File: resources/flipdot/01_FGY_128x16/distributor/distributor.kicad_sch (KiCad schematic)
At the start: 46 parts, among them J1 Conn_01x34, J2 Conn_01x28, J3 Conn_01x16, J4 Conn_01x16, U1 4049, U10 4051, U11 4051, U12 4051, U13 UDN2580, U14 UDN2580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

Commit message: Distributor board design files v0.2
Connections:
- net column_b3 renamed column_bank_b0
- net column_b4 renamed column_bank_b1
- net column_b5 renamed column_bank_b2
- net column_b6 renamed column_bank_b3
- net column_b6_{+1} renamed column_bank_b3_{+1}
- net column_e? renamed flip_enable
- net column_e?_{+1} renamed column_enable
- net column_~{b6}_{+1} renamed column_bank_~{b3}_{+1}
- net column_~{e}?_{+2} renamed row_bank_select_inh
- net mode_0? renamed model_select_0?
- net mode_1? renamed model_select_1?
- net mode_2? renamed model_select_2?
- net mode_3? renamed model_select_3?
- net mode_4? renamed model_select_4?
- net mode_5? renamed model_select_5?
- net mode_6? renamed model_select_6?
- net mode_7? renamed model_select_7?
- net row_bnk_0_inh renamed row_bank_0_inh
- net row_bnk_1_inh renamed row_bank_1_inh
- net row_bnk_2_inh renamed row_bank_2_inh
- net row_inhibit? renamed row_dir_source
- net row_inhibit?_{+1} renamed row_dir_drain
- net unk0 renamed column_dir_drain
- net unk1 renamed column_dir_source
- net unk2 renamed flip_dir
- net weird renamed row_bank_disable_all
- net weird_{+1} renamed row_bank_disable_all_{+1}
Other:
- note added: "VIBRATOR"
- note added: "[0..4]"
- note added: "[16..18]"
- note added: "[24..31]"
- note added: "[7..11]"
- note added: "[7]"
- moved on the sheet: C1, C10, C11, C12, C13, C2, C3, C4, C5, C7, C8, C9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

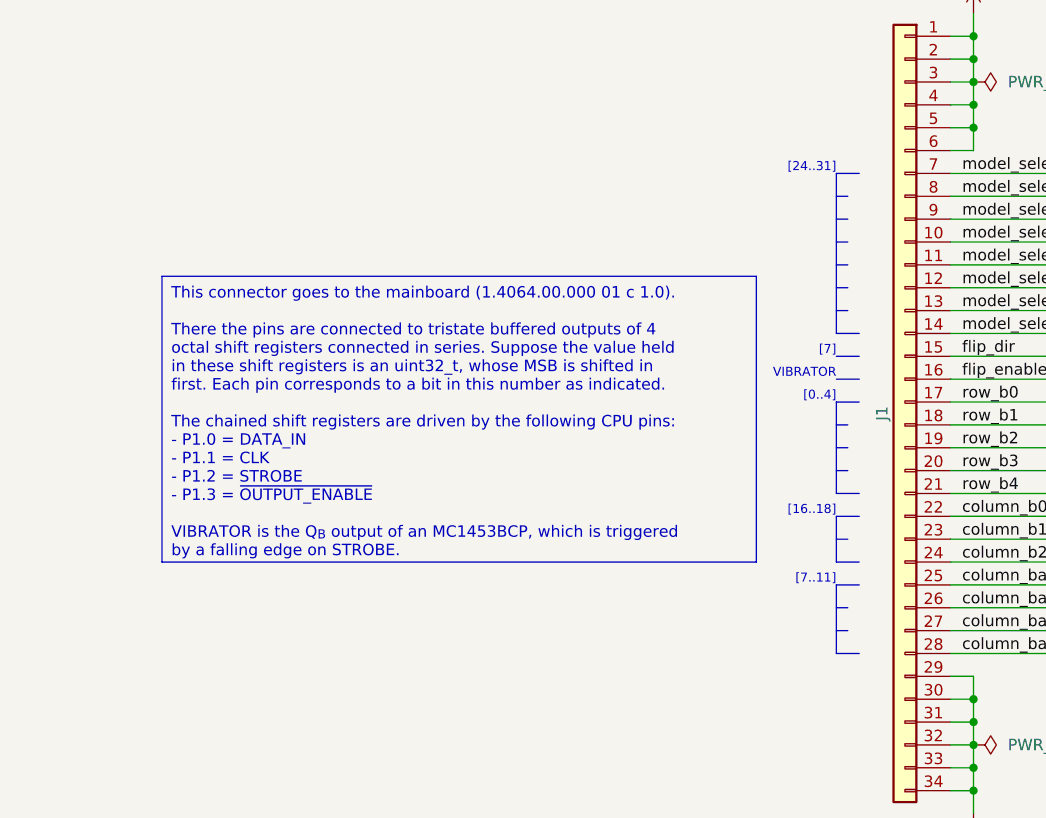
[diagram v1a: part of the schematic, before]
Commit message: Documentation correction, firmware now works with multiple panels
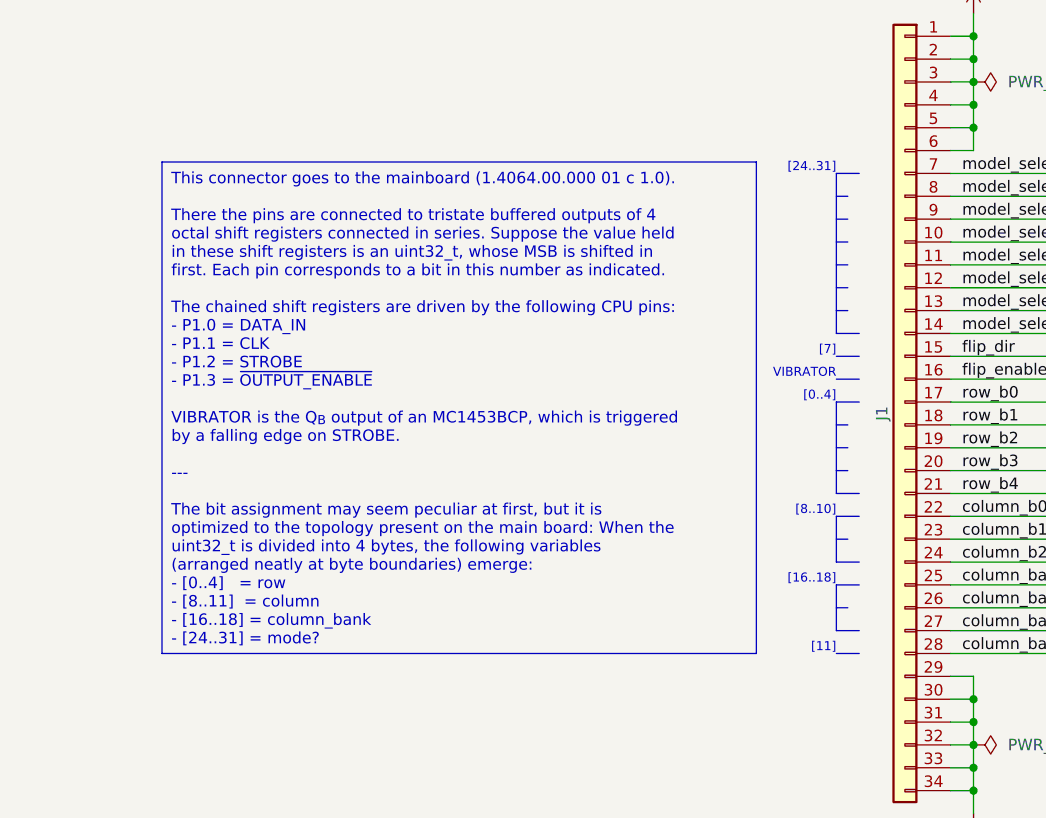
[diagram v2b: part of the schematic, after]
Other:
- note added: "[11]"
- note added: "[8..10]"
- note removed: "[7..11]"
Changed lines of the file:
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@@
   (title_block
     (title "FOK-GYEM 1 4070 c 2.0 (replica)")
-    (date "2023-07-30")
-    (rev "0.2")
+    (date "2023-08-03")
+    (rev "0.3")
     (comment 1 "OF MERCHANTABILITY, FITNESS FOR A PARTICULAR PURPOSE AND NONINFRINGEMENT.")
     (comment 2 "EXPRESS OR IMPLIED, INCLUDING BUT NOT LIMITED TO THE WARRANTIES")
@@
     (stroke (width 0.75) (type default))
   )
-  (polyline (pts (xy 109.22 130.81) (xy 109.22 138.43))
+  (polyline (pts (xy 109.22 130.81) (xy 109.22 135.89))
     (stroke (width 0) (type default))
   )
@@
     (stroke (width 0) (type default))
   )
+  (polyline (pts (xy 109.22 138.43) (xy 111.76 138.43))
+    (stroke (width 0) (type default))
+  )
   (wire (pts (xy 142.24 318.77) (xy 142.24 320.04))
     (stroke (width 0) (type default))
@@
   )
   (polyline (pts (xy 109.22 87.63) (xy 110.49 87.63))
-    (stroke (width 0) (type default))
-  )
-  (polyline (pts (xy 109.22 135.89) (xy 110.49 135.89))
     (stroke (width 0) (type default))
   )
@@
     (stroke (width 0) (type default))
   )
-  (polyline (pts (xy 109.22 138.43) (xy 111.76 138.43))
+  (polyline (pts (xy 109.22 135.89) (xy 111.76 135.89))
     (stroke (width 0) (type default))
   )
@@
     (effects (font (size 1.27 1.27)) (justify left top))
   )
-  (text_box "This connector goes to the mainboard (1.4064.00.000 01 c 1.0).\n\nThere the pins are connected to tristate buffered outputs of 4 octal shift registers connected in series. Suppose the value held in these shift registers is an uint32_t, whose MSB is shifted in first. Each pin corresponds to a bit in this number as indicated.\n\nThe chained shift registers are driven by the following CPU pins:\n- P1.0 = DATA_IN\n- P1.1 = CLK\n- P1.2 = STROBE\n- P1.3 = ~{OUTPUT_ENABLE}\n\nVIBRATOR is the Q_{B} output of an MC1453BCP, which is triggered by a falling edge on STROBE."
-    (at 34.29 96.52 0) (size 66.04 31.75)
+  (text_box "This connector goes to the mainboard (1.4064.00.000 01 c 1.0).\n\nThere the pins are connected to tristate buffered outputs of 4 octal shift registers connected in series. Suppose the value held in these shift registers is an uint32_t, whose MSB is shifted in first. Each pin corresponds to a bit in this number as indicated.\n\nThe chained shift registers are driven by the following CPU pins:\n- P1.0 = DATA_IN\n- P1.1 = CLK\n- P1.2 = STROBE\n- P1.3 = ~{OUTPUT_ENABLE}\n\nVIBRATOR is the Q_{B} output of an MC1453BCP, which is triggered by a falling edge on STROBE.\n\n---\n\nThe bit assignment may seem peculiar at first, but it is optimized to the topology present on the main board: When the uint32_t is divided into 4 bytes, the following variables (arranged neatly at byte boundaries) emerge:\n- [0..4]   = row\n- [8..11]  = column\n- [16..18] = column_bank\n- [24..31] = mode?"
+    (at 34.29 83.82 0) (size 66.04 54.61)
     (stroke (width 0) (type default))
     (fill (type none))
@@
     (effects (font (size 1 1)) (justify right bottom))
   )
-  (text "[16..18]" (at 109.22 123.19 0)
+  (text "[8..10]" (at 109.22 123.19 0)
     (effects (font (size 1 1)) (justify right bottom))
   )
@@
     (effects (font (size 1 1)) (justify right bottom))
   )
-  (text "[7..11]" (at 109.22 130.81 0)
+  (text "[16..18]" (at 109.22 130.81 0)
     (effects (font (size 1 1)) (justify right bottom))
   )
@@
     (effects (font (size 1 1)) (justify right bottom))
   )
+  (text "[11]" (at 109.22 138.43 0)
+    (effects (font (size 1 1)) (justify right bottom))
+  )
